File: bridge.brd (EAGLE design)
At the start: 62.2 x 25.7 mm, 2 parts, among them P1 HEADERS23-2, P2 HEADERS23-2

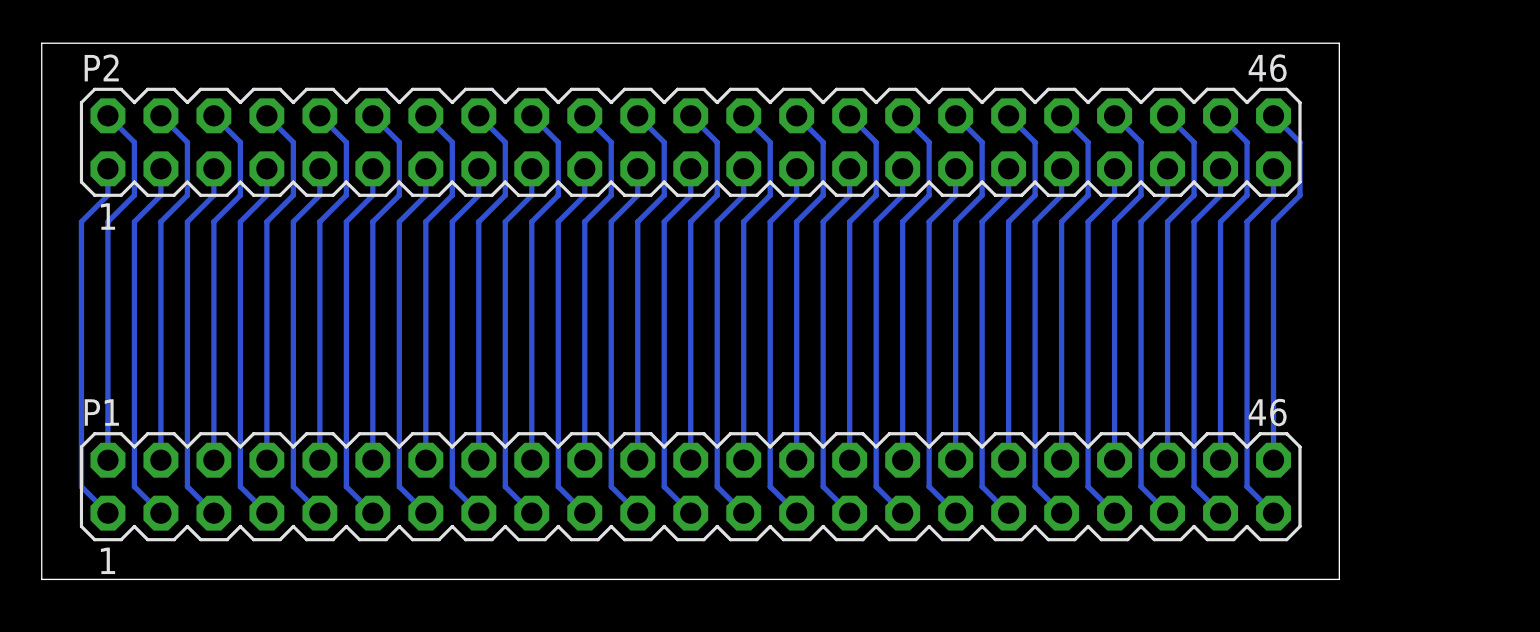
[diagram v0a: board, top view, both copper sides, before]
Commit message: Offset bridge connector
This is necessary if I want to put the TOSLINK connector right through
the chassis.
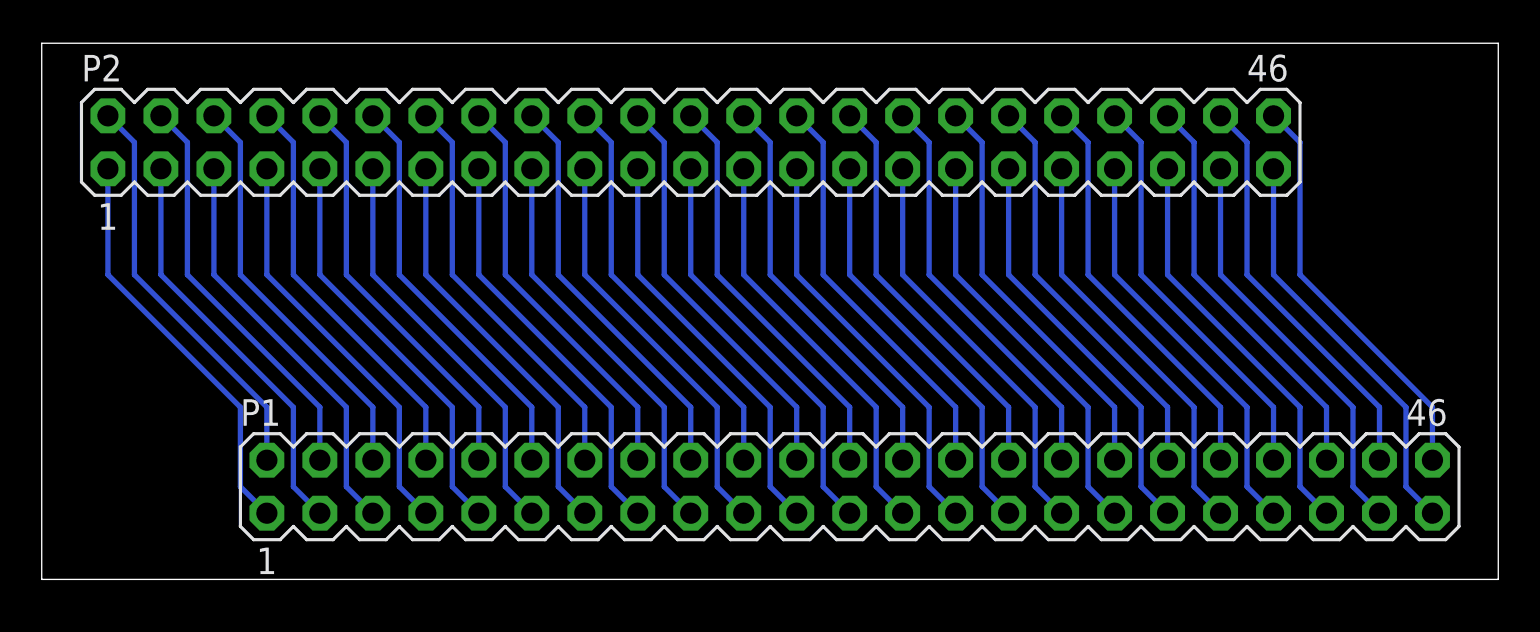
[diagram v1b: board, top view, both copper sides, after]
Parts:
- moved P1 7.62 mm to (34.9, 4.45)
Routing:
- net N$18: track 17.6 -> 19.7 mm
- net N$17: track 17.6 -> 19.7 mm
- net N$16: track 17.6 -> 19.7 mm
- net N$8: track 17.6 -> 19.7 mm
- net N$7: track 17.6 -> 19.7 mm
- net N$45: track 17.6 -> 19.7 mm
- net N$6: track 17.6 -> 19.7 mm
- net N$35: track 17.6 -> 19.7 mm
- net N$34: track 17.6 -> 19.7 mm
- net N$33: track 17.6 -> 19.7 mm
- net N$30: track 17.6 -> 19.7 mm
- net N$29: track 17.6 -> 19.7 mm
- net N$27: track 17.6 -> 19.7 mm
- net N$26: track 17.6 -> 19.7 mm
- net N$25: track 17.6 -> 19.7 mm
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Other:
- board size 62.2 x 25.7 mm -> 69.8 x 25.7 mm

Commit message: Move the top row of the bridge down a bit
This makes it fit four times in 10 cm.

Also made a panelized version of the board.
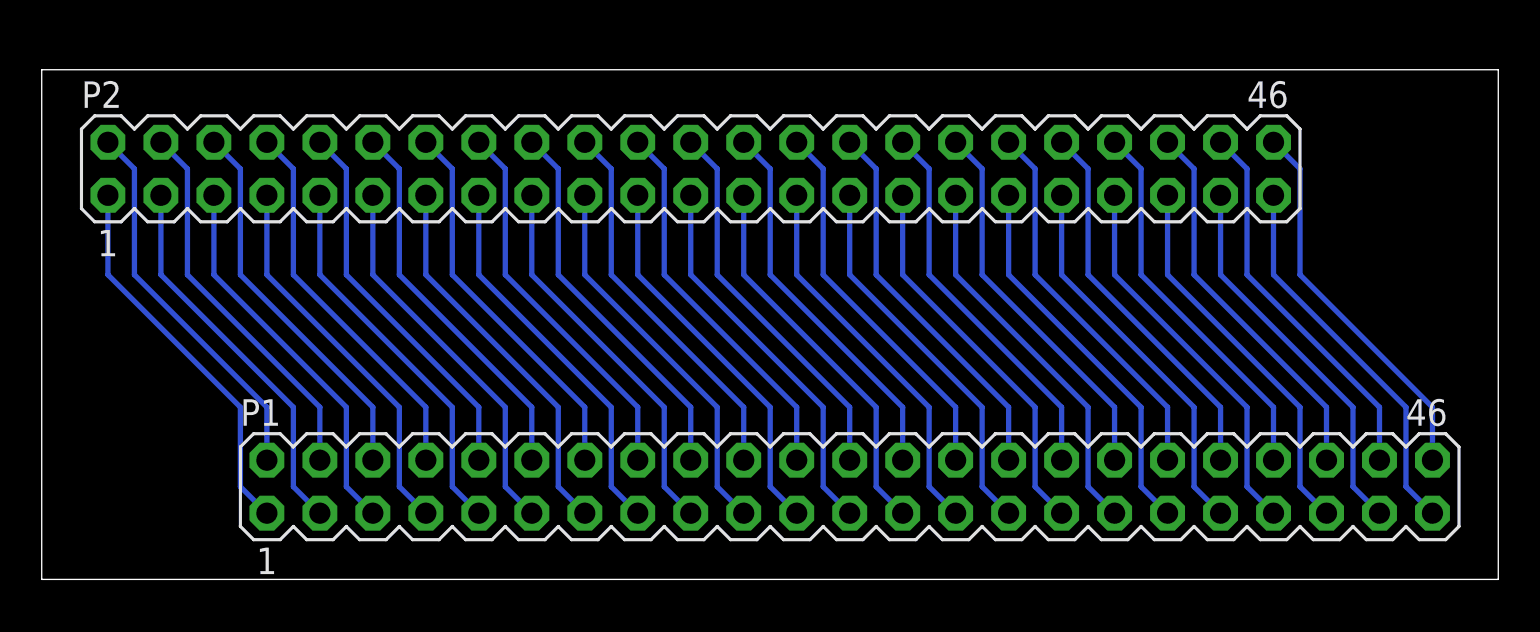
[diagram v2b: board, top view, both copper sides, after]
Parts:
- moved P2 1.27 mm to (27.3, 19.7)
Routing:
- net N$8: track 19.7 -> 18.4 mm
- net N$7: track 19.7 -> 18.4 mm
- net N$45: track 19.7 -> 18.4 mm
- net N$41: track 19.7 -> 18.4 mm
- net N$40: track 19.7 -> 18.4 mm
- net N$39: track 19.7 -> 18.4 mm
- net N$35: track 19.7 -> 18.4 mm
- net N$34: track 19.7 -> 18.4 mm
- net N$33: track 19.7 -> 18.4 mm
- net N$31: track 19.7 -> 18.4 mm
- net N$30: track 19.7 -> 18.4 mm
- net N$29: track 19.7 -> 18.4 mm
- net N$27: track 19.7 -> 18.4 mm
- net N$26: track 19.7 -> 18.4 mm
- net N$25: track 19.7 -> 18.4 mm
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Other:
- board size 69.8 x 25.7 mm -> 69.8 x 24.4 mm

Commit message: Mirrored the offset of the bridge connector
I made a very stupid mistake and offset it the wrong direction. I
thought I accounted for the board being upside-down, but I messed up...
Hours of work down the drain.
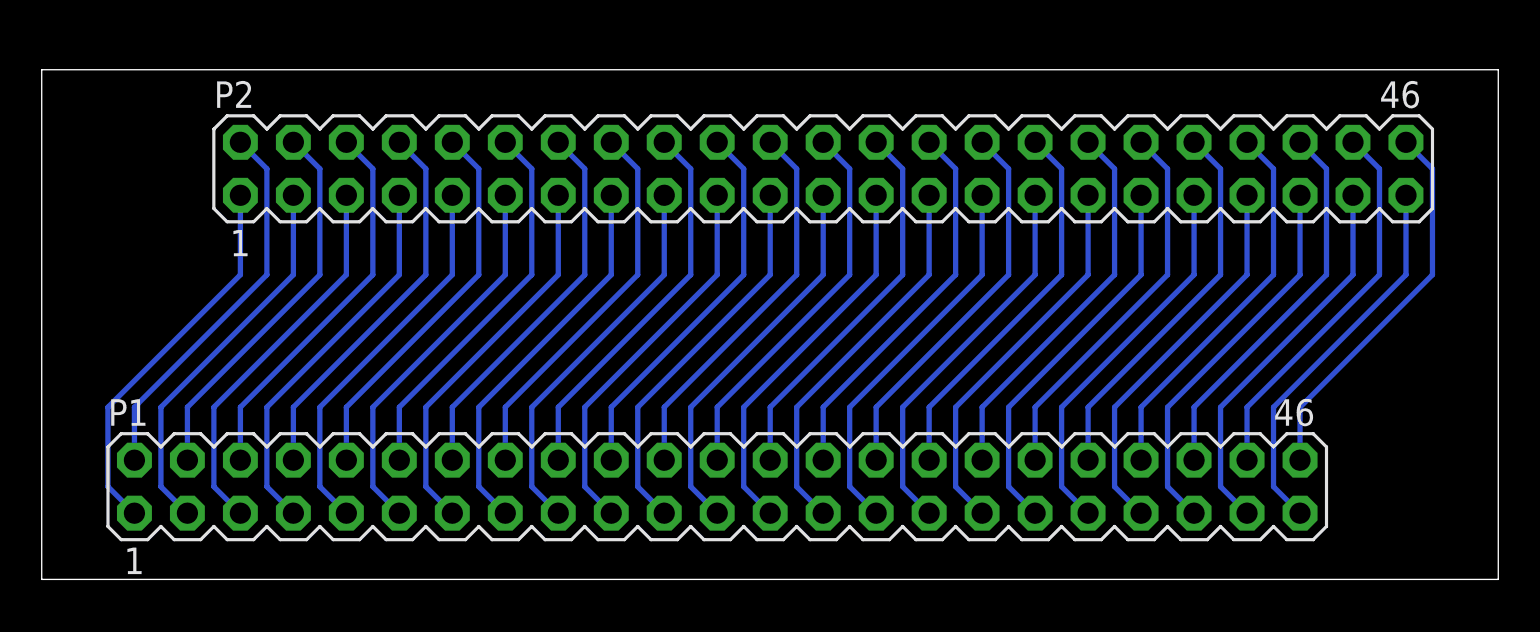
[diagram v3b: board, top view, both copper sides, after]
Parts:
- moved P2 6.35 mm to (33.7, 19.7)
- moved P1 6.35 mm to (28.6, 4.45)

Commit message: Add ground plane to bridge
This creates nice 50 Ohm impedance transmission lines (ish).
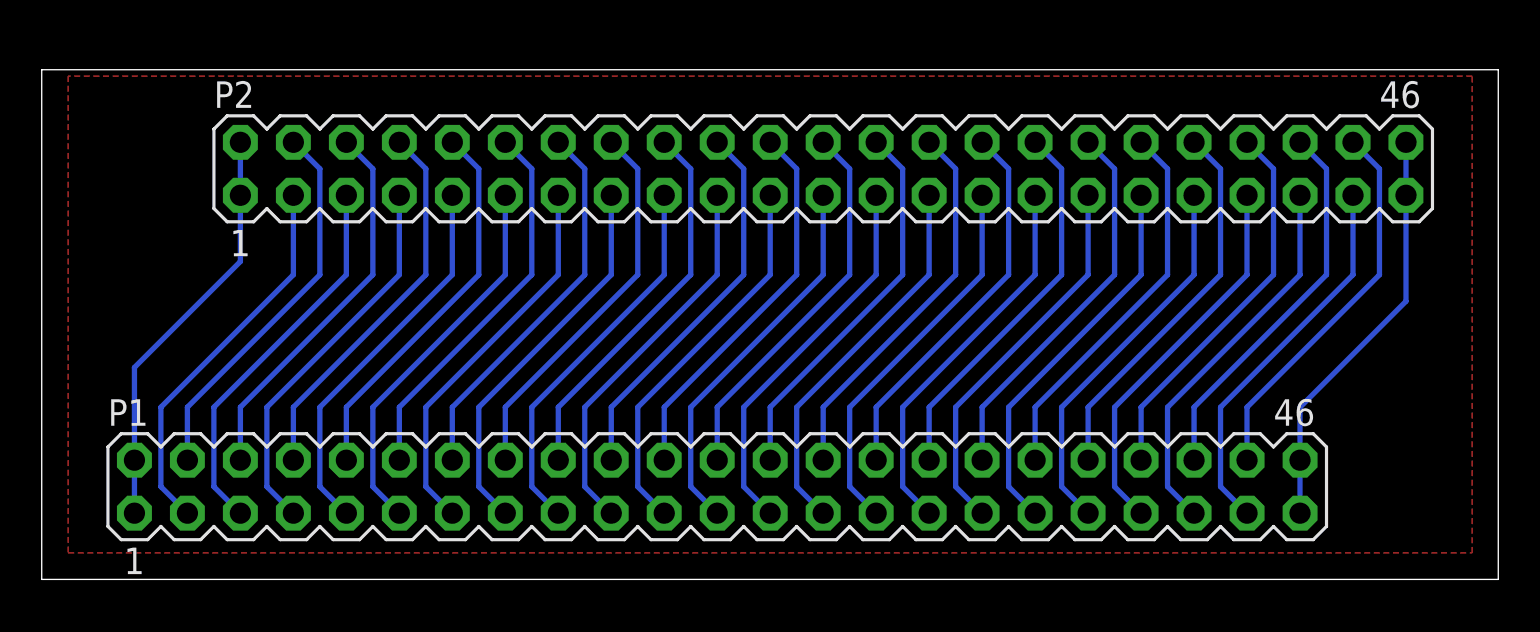
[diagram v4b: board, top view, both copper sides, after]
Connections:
- removed net N$1: P1.1, P2.1
- removed net N$23: P1.45, P2.45
- removed net N$24: P1.2, P2.2
- removed net N$46: P1.46, P2.46
- new net GND: P1.1, P1.2, P1.45, P1.46, P2.1, P2.2, P2.45, P2.46
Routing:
- net GND: track 0.00 -> 39.8 mm
- net N$23: track 18.4 -> 0.00 mm
- net N$24: track 18.4 -> 0.00 mm
- net N$1: track 18.4 -> 0.00 mm
- net N$46: track 18.4 -> 0.00 mm
- added copper zone on layer 1, net GND
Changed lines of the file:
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@@
 </elements>
 <signals>
-<signal name="N$1">
+<signal name="GND">
 <contactref element="P1" pad="1"/>
 <contactref element="P2" pad="1"/>
-<wire x1="4.445" y1="3.175" x2="3.175" y2="4.445" width="0.254" layer="16"/>
-<wire x1="3.175" y1="4.445" x2="3.175" y2="8.255" width="0.254" layer="16"/>
-<wire x1="3.175" y1="8.255" x2="9.525" y2="14.605" width="0.254" layer="16"/>
-<wire x1="9.525" y1="14.605" x2="9.525" y2="18.415" width="0.254" layer="16"/>
+<contactref element="P1" pad="2"/>
+<contactref element="P2" pad="2"/>
+<wire x1="4.445" y1="3.175" x2="4.445" y2="5.715" width="0.254" layer="16"/>
+<wire x1="4.445" y1="5.715" x2="4.445" y2="10.16" width="0.254" layer="16"/>
+<wire x1="4.445" y1="10.16" x2="9.525" y2="15.24" width="0.254" layer="16"/>
+<wire x1="9.525" y1="15.24" x2="9.525" y2="18.415" width="0.254" layer="16"/>
+<wire x1="9.525" y1="18.415" x2="9.525" y2="20.955" width="0.254" layer="16"/>
+<polygon width="0.4064" layer="1">
+<vertex x="1.27" y="24.13"/>
+<vertex x="1.27" y="1.27"/>
+<vertex x="68.58" y="1.27"/>
+<vertex x="68.58" y="24.13"/>
+</polygon>
+<contactref element="P1" pad="45"/>
+<contactref element="P2" pad="45"/>
+<contactref element="P1" pad="46"/>
+<contactref element="P2" pad="46"/>
+<wire x1="60.325" y1="3.175" x2="60.325" y2="5.715" width="0.254" layer="16"/>
+<wire x1="60.325" y1="5.715" x2="60.325" y2="8.255" width="0.254" layer="16"/>
+<wire x1="60.325" y1="8.255" x2="65.405" y2="13.335" width="0.254" layer="16"/>
+<wire x1="65.405" y1="13.335" x2="65.405" y2="18.415" width="0.254" layer="16"/>
+<wire x1="65.405" y1="18.415" x2="65.405" y2="20.955" width="0.254" layer="16"/>
 </signal>
 <signal name="N$2">
@@
 <wire x1="56.515" y1="8.255" x2="56.515" y2="4.445" width="0.254" layer="16"/>
 </signal>
-<signal name="N$23">
-<contactref element="P1" pad="45"/>
-<contactref element="P2" pad="45"/>
-<wire x1="60.325" y1="3.175" x2="59.055" y2="4.445" width="0.254" layer="16"/>
-<wire x1="65.405" y1="18.415" x2="65.405" y2="14.605" width="0.254" layer="16"/>
-<wire x1="65.405" y1="14.605" x2="59.055" y2="8.255" width="0.254" layer="16"/>
-<wire x1="59.055" y1="8.255" x2="59.055" y2="4.445" width="0.254" layer="16"/>
-</signal>
-<signal name="N$24">
-<contactref element="P1" pad="2"/>
-<contactref element="P2" pad="2"/>
-<wire x1="9.525" y1="20.955" x2="10.795" y2="19.685" width="0.254" layer="16"/>
-<wire x1="10.795" y1="19.685" x2="10.795" y2="14.605" width="0.254" layer="16"/>
-<wire x1="4.445" y1="8.255" x2="4.445" y2="5.715" width="0.254" layer="16"/>
-<wire x1="10.795" y1="14.605" x2="4.445" y2="8.255" width="0.254" layer="16"/>
-</signal>
 <signal name="N$25">
 <contactref element="P1" pad="4"/>
@@
 <wire x1="57.785" y1="8.255" x2="57.785" y2="5.715" width="0.254" layer="16"/>
 </signal>
-<signal name="N$46">
-<contactref element="P1" pad="46"/>
-<contactref element="P2" pad="46"/>
-<wire x1="66.675" y1="19.685" x2="65.405" y2="20.955" width="0.254" layer="16"/>
-<wire x1="66.675" y1="19.685" x2="66.675" y2="14.605" width="0.254" layer="16"/>
-<wire x1="66.675" y1="14.605" x2="60.325" y2="8.255" width="0.254" layer="16"/>
-<wire x1="60.325" y1="8.255" x2="60.325" y2="5.715" width="0.254" layer="16"/>
-</signal>
 </signals>
